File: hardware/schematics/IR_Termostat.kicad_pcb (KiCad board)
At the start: 2 copper layers, 30.5 x 64.5 mm, 40 parts, among them J1 USB_C_Receptacle_PowerOnly_6P, J2 JST-PH-2mm, J3 Conn_01x03_Pin, Q1 FDN306P, SW1 SW_SPST, U1 TP4056-42-ESOP8, U2 XC6206P-3.3V, U4 MLX90614ESF-BAA-000-TU, U5 CH32V003JxMx

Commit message: Fix: Battery mensurement circuit upgrade
Better Iq by 100x and a capacitor to filter noises, also refresh the pcb
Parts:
- added C9: 100nF 16V, Capacitor_SMD:C_0805_2012Metric_Pad1.18x1.45mm_HandSolder, F.Cu at (163.0, 107.0)
- D1: value SSL14 -> PMEG2005EH; footprint Diode_SMD:D_SMA_Handsoldering -> Diode_SMD:D_SOD-123F
- R11: value 22K 1% -> 2M 1%
- R12: value 9.1K 1% -> 1M 1%
- U2: value XC6206P-3.3V -> TPS7A0233DBVR; footprint Package_TO_SOT_SMD:SOT-23-3 -> Package_TO_SOT_SMD:SOT-23-5
- U3: value ~ -> XB8089D
- moved R11 0.50 mm to (161.0, 109.0)
- moved R12 0.50 mm to (165.0, 109.0)
- moved U2 0.25 mm to (153.0, 116.9)
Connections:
- U2 pad 1: GND -> Net-(D1-K)
- U2 pad 2: +3.3V -> GND
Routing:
- net +3.3V: track 115.1 -> 131.9 mm
- net GND: track 113.3 -> 123.2 mm, vias 17 -> 18
- net Net-(D1-K): track 12.4 -> 18.1 mm
- net +5V: track 61.1 -> 63.7 mm, vias 2 -> 4
- net Net-(U5-PD6/PA1): track 16.7 -> 18.8 mm
- net Net-(U5-PA2): track 20.1 -> 19.3 mm

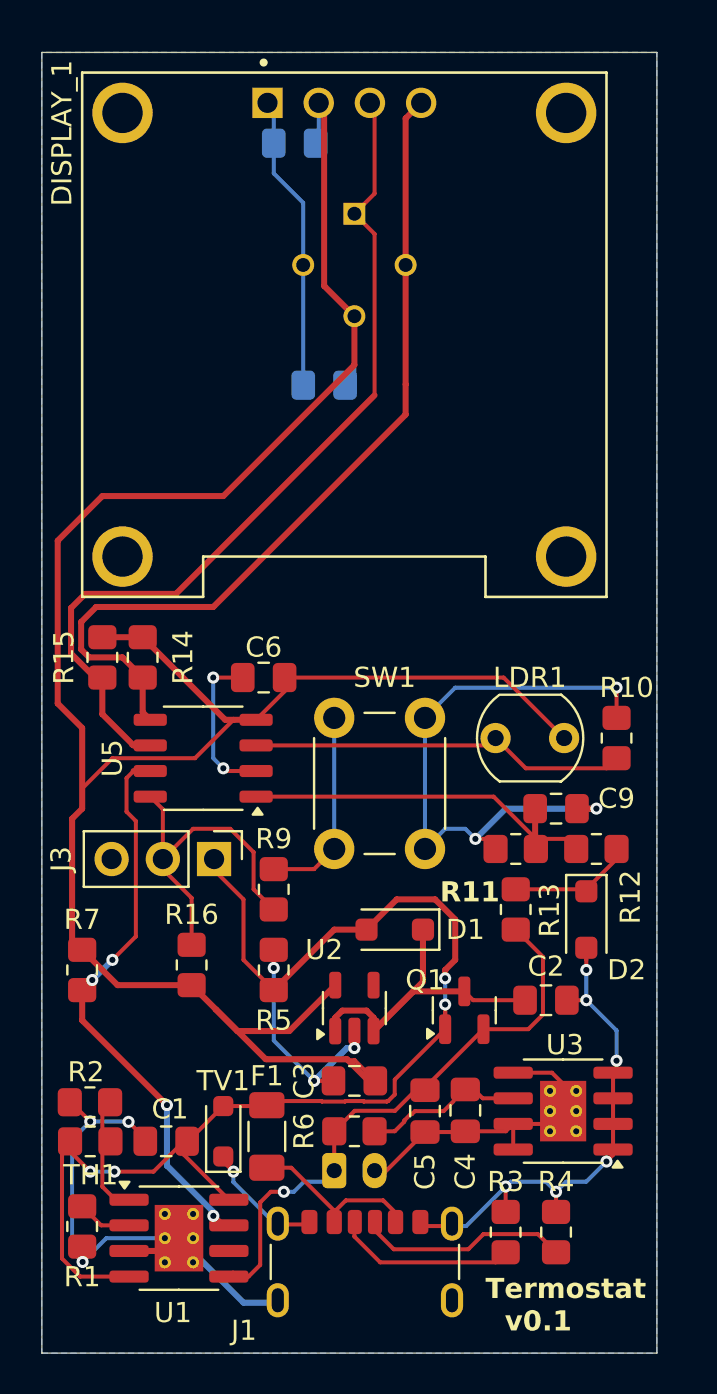
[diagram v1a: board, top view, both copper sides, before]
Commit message: fix: schematic datasheets fixed, and docs upgrade by realises
Now the BOM it's up-to-date with the schematic datasheets by versions
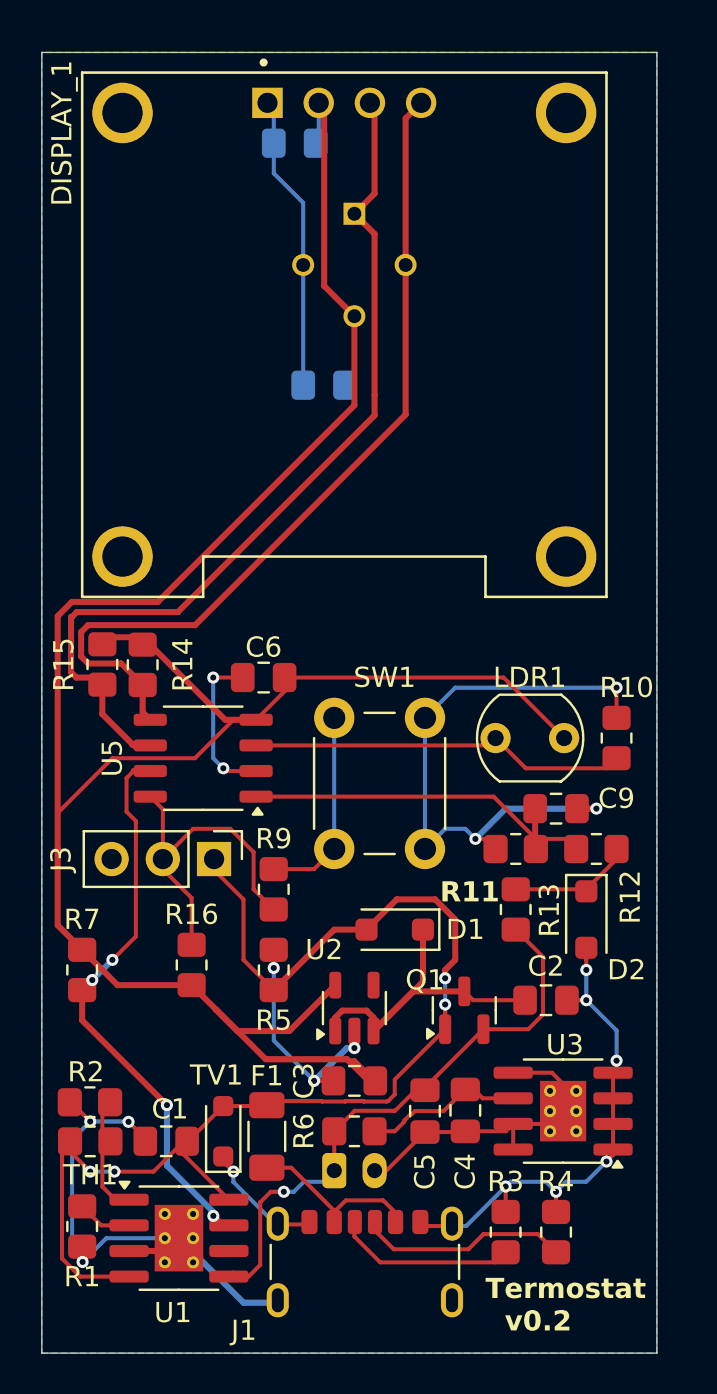
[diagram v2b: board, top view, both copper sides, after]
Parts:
- moved R14 0.37 mm to (142.5, 99.9)
- moved R15 0.35 mm to (140.5, 99.9)
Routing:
- net +3.3V: track 131.9 -> 133.0 mm
- net SCL: track 44.9 -> 45.8 mm
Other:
- board text added: "Termostat v0.2"
- board text removed: "Termostat v0.1"

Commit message: Fix: LCSC Compliance
This commit fix the pcb, branching a new version v0.3, thats it's side-by-side with the LCSC DFM check
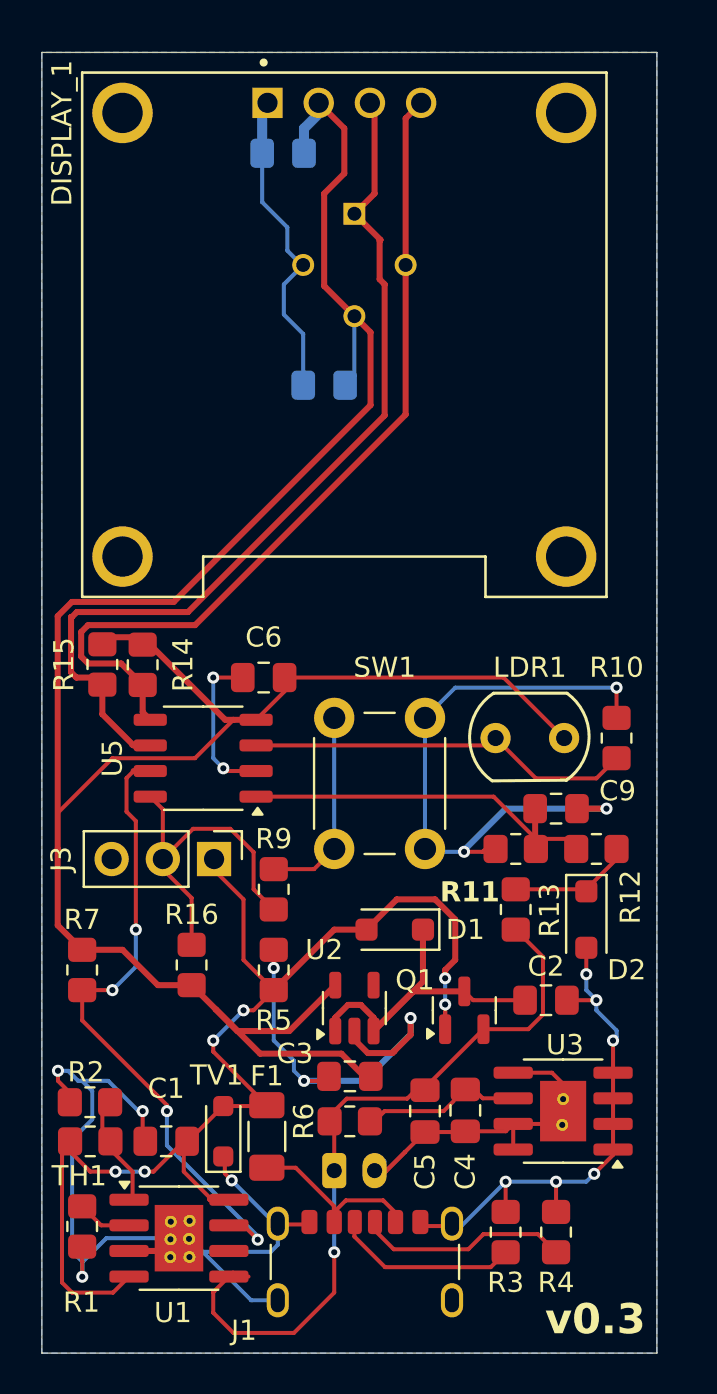
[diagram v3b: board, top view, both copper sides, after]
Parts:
- moved C8 0.76 mm to (149.5, 74.5)
- moved R6 0.54 mm to (152.8, 122.5)
- moved C3 0.32 mm to (152.8, 120.3)
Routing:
- net GND: track 123.2 -> 149.7 mm
- net +3.3V: track 133.0 -> 125.3 mm
- net Vbat+: track 29.7 -> 36.7 mm
- net CHRG: track 28.5 -> 32.7 mm
- net Net-(J2-Pin_2): track 16.7 -> 19.3 mm
- net Net-(U1-TEMP): track 4.99 -> 6.34 mm
- net SCL: track 45.8 -> 46.5 mm
- net +5V: track 63.7 -> 63.3 mm, vias 4 -> 6
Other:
- board text added: "v0.3"
- board text removed: "BATTERY"
- board text removed: "Termostat v0.2"
